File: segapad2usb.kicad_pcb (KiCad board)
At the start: 2 copper layers, 55 x 90 mm, 14 parts, among them J1 DB9_MALE_SEGA, J2 Conn_02x04_Odd_Even, SW1 RST, U1 Arduino_Pro_Micro

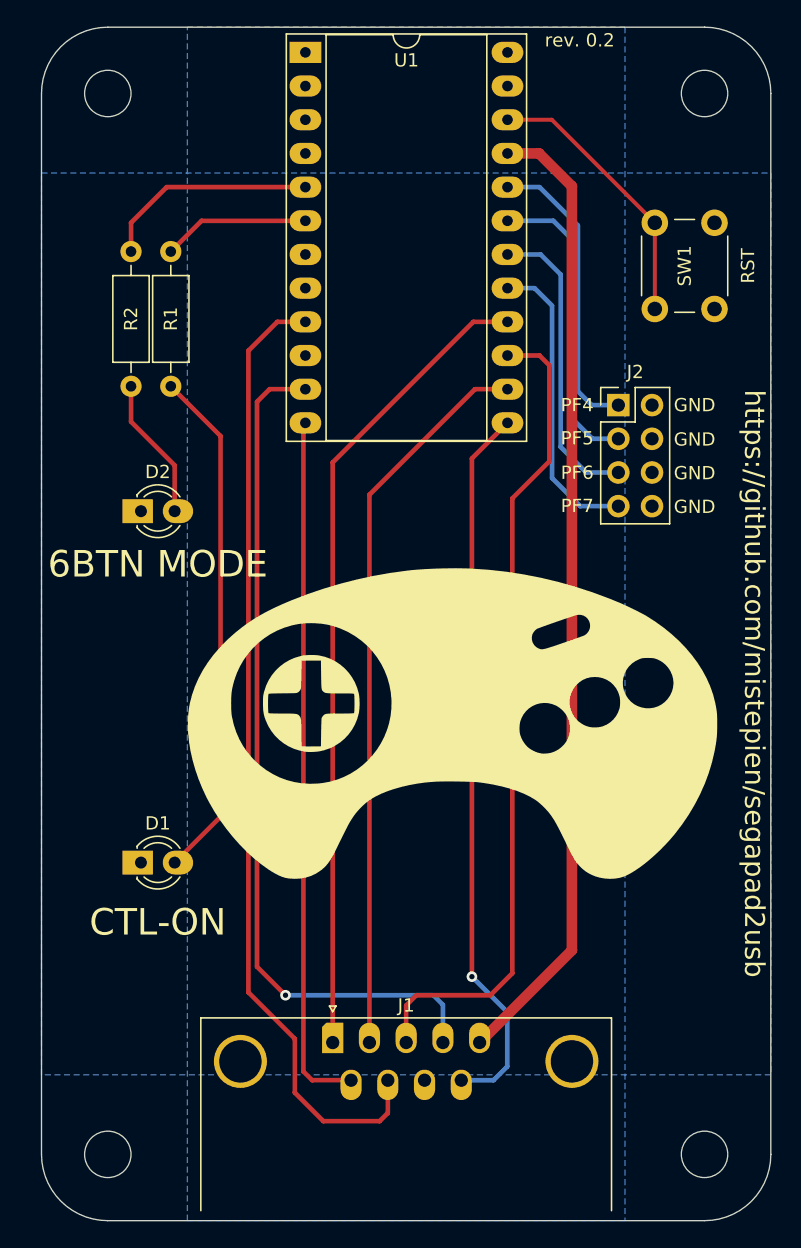
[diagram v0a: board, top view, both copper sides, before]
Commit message: PCB Rev. 0.4
- GND zone on both sides of pcb
- status led
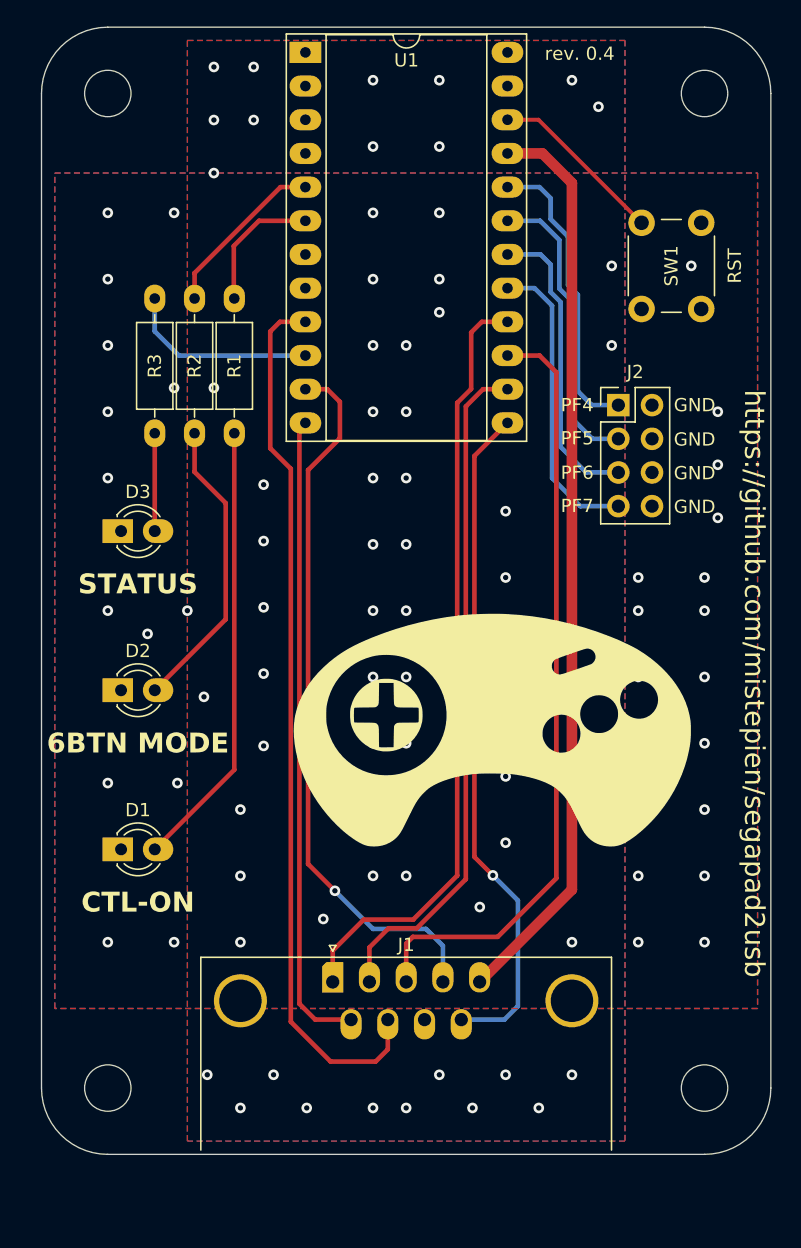
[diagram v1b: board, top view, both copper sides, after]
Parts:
- removed the G*** at (91.0, 98.5)
- added D3: STATUS, misc:LED_D3.0mm_Oval, F.Cu at (66.0, 84.0)
- added G***: LOGO, misc:md_gamepad_30x17mm, F.Cu at (94.0, 99.0)
- added R3: RxΩ, misc:R_Axial_DIN0207_L6.3mm_D2.5mm_P10.16mm_Horizontal_Oval, F.Cu at (68.5, 66.5)
- D1, D2: footprint Misc:LED_D3.0mm_Oval -> misc:LED_D3.0mm_Oval
- R1, R2: value R470Ω -> RxΩ; footprint Resistor_THT:R_Axial_DIN0207_L6.3mm_D2.5mm_P10.16mm_Horizontal -> misc:R_Axial_DIN0207_L6.3mm_D2.5mm_P10.16mm_Horizontal_Oval
- moved H1 91.8 mm to (110.0, 51.0)
- moved H3 87.5 mm to (110.0, 126.0)
- moved H4 45.3 mm to (65.0, 126.0)
- moved H2 45.0 mm to (65.0, 51.0)
- moved D2 13.6 mm to (66.0, 96.0)
- moved REF** 6.31 mm to (89.4, 95.1)
- moved R1 5.96 mm to (74.5, 66.5)
- moved R2 5.96 mm to (71.5, 66.5)
- moved J1 4.57 mm to (82.0, 118.0)
- moved D1 1.80 mm to (66.0, 108.0)
- moved SW1 1.00 mm to (105.2, 67.2)
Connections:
- U1 pad 10: unconnected-(U1-Pad10) -> /STATUSLED
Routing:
- net /STATUSLED: track 0.00 -> 14.6 mm
- net Net-(D2-A): track 10.8 -> 22.6 mm
- net /DB9_PIN_4: track 64.7 -> 54.3 mm
- net /RST: track 21.0 -> 13.3 mm
- net Net-(D3-A): track 0.00 -> 7.38 mm
- net /DB9_SELECT_PIN: track 73.2 -> 66.8 mm
- net Net-(D1-A): track 38.9 -> 34.0 mm
- net /DB9_PIN_6: track 52.8 -> 48.4 mm
- net VCC: track 73.3 -> 68.9 mm
- net /DB9_PIN_2: track 55.0 -> 51.3 mm
- net /DB9_PIN_3: track 62.3 -> 58.6 mm
- net /DB9_PIN_9: track 54.6 -> 51.1 mm
- net /MODELED: track 16.4 -> 13.0 mm
- net /DB9_PIN_1: track 61.3 -> 58.6 mm
- net /CTL-LED: track 11.1 -> 10.2 mm
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- added copper zone on F.Cu, net GND
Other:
- board size 55 x 90 mm -> 55 x 85 mm

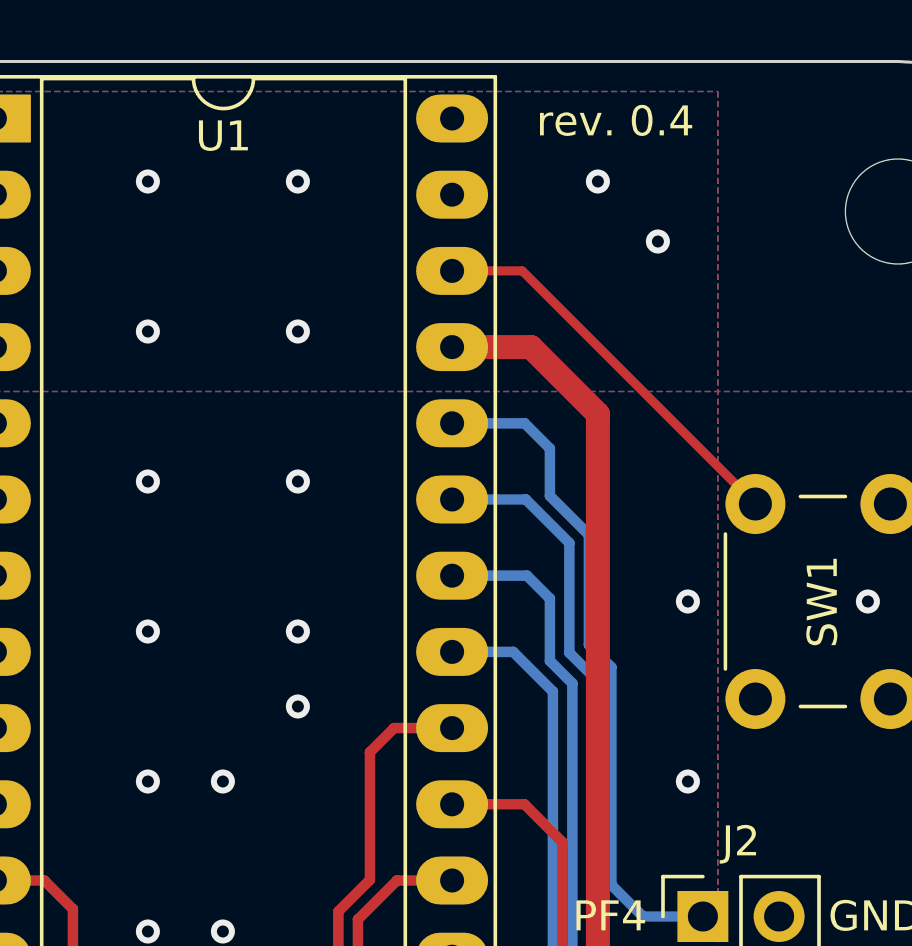
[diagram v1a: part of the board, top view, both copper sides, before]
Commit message: PCB Rev. 0.5
pcb will be cheaper in JLCPCB
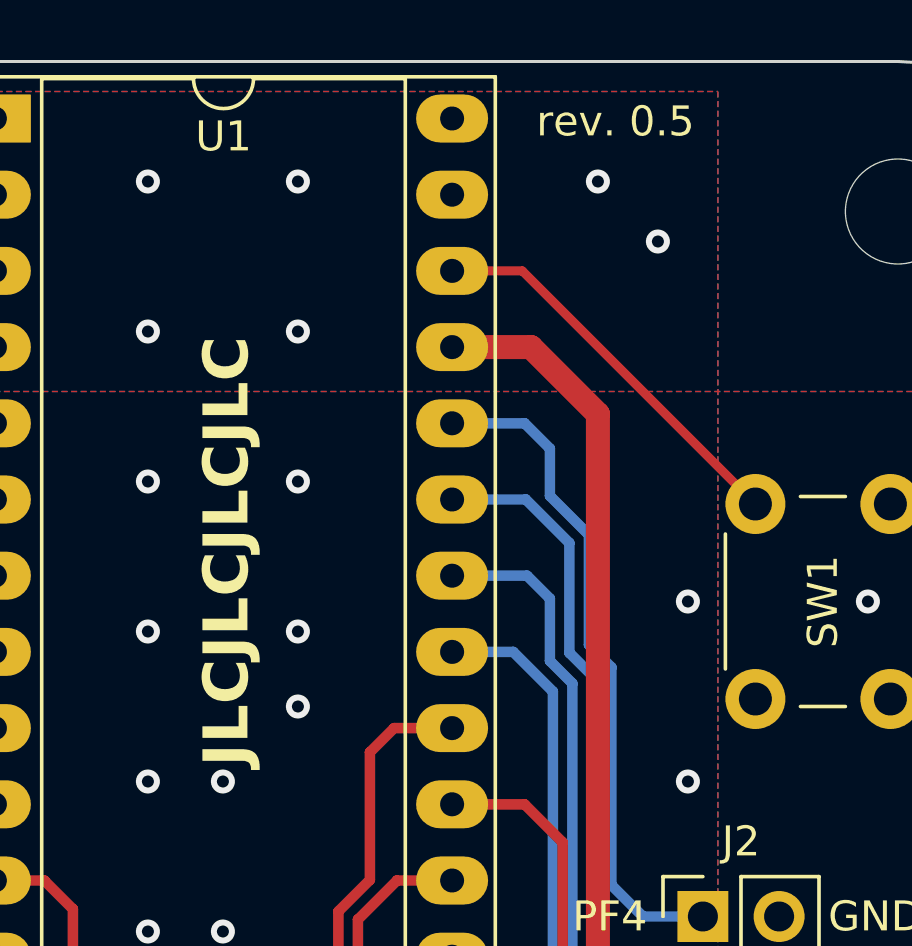
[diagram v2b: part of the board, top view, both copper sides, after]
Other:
- board text added: "JLCJLCJLCJLC"
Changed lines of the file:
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@@
   (title_block
     (title "segapad2usb")
-    (rev "0.4")
-    (company "mistepien")
+    (rev "0.5")
+    (company "mistepien@wp.pl")
   )
   (layers
@@
     (effects (font (size 1 1) (thickness 0.15)))
   )
+  (gr_text "JLCJLCJLCJLC" (at 88.5 69.5 90) (layer "F.SilkS")
+    (effects (font (size 1.5 1.5) (thickness 0.3) bold) (justify left bottom))
+  )
   (dimension (type aligned) (layer "Dwgs.User")

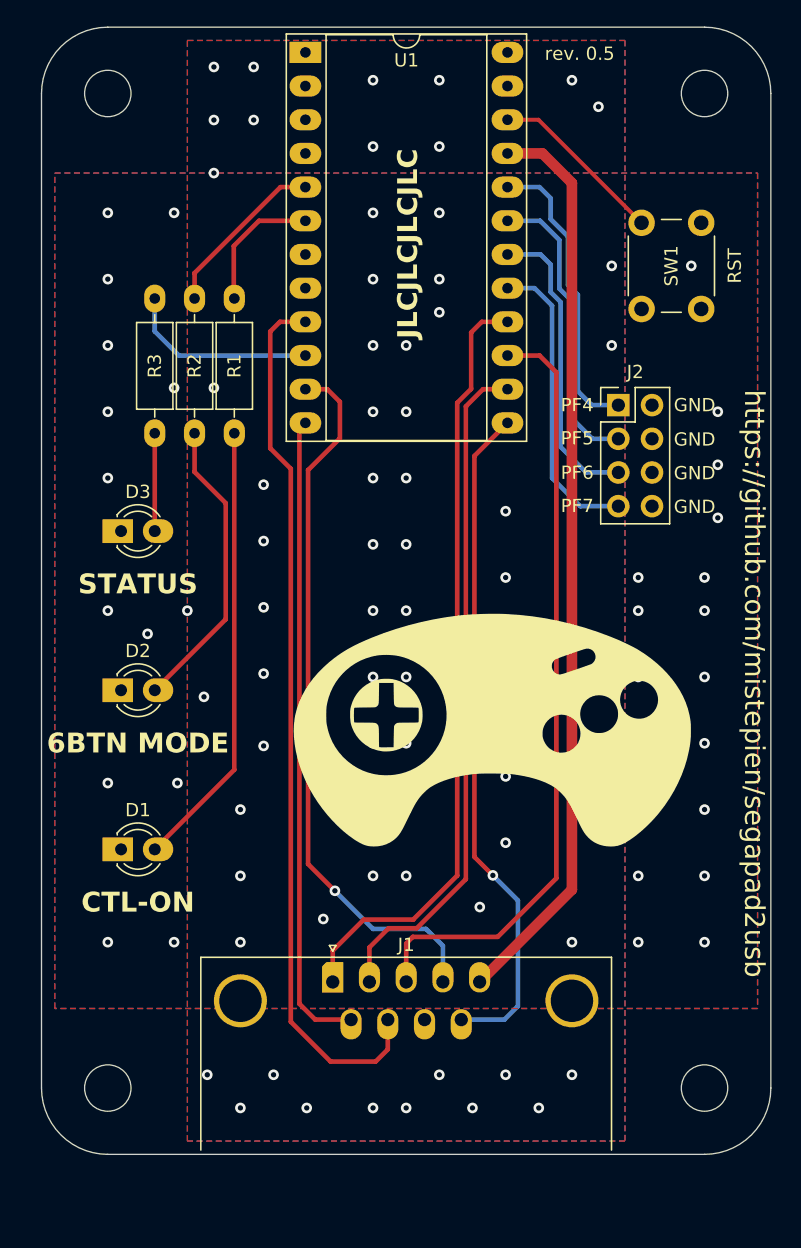
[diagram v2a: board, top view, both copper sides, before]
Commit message: added teardrops
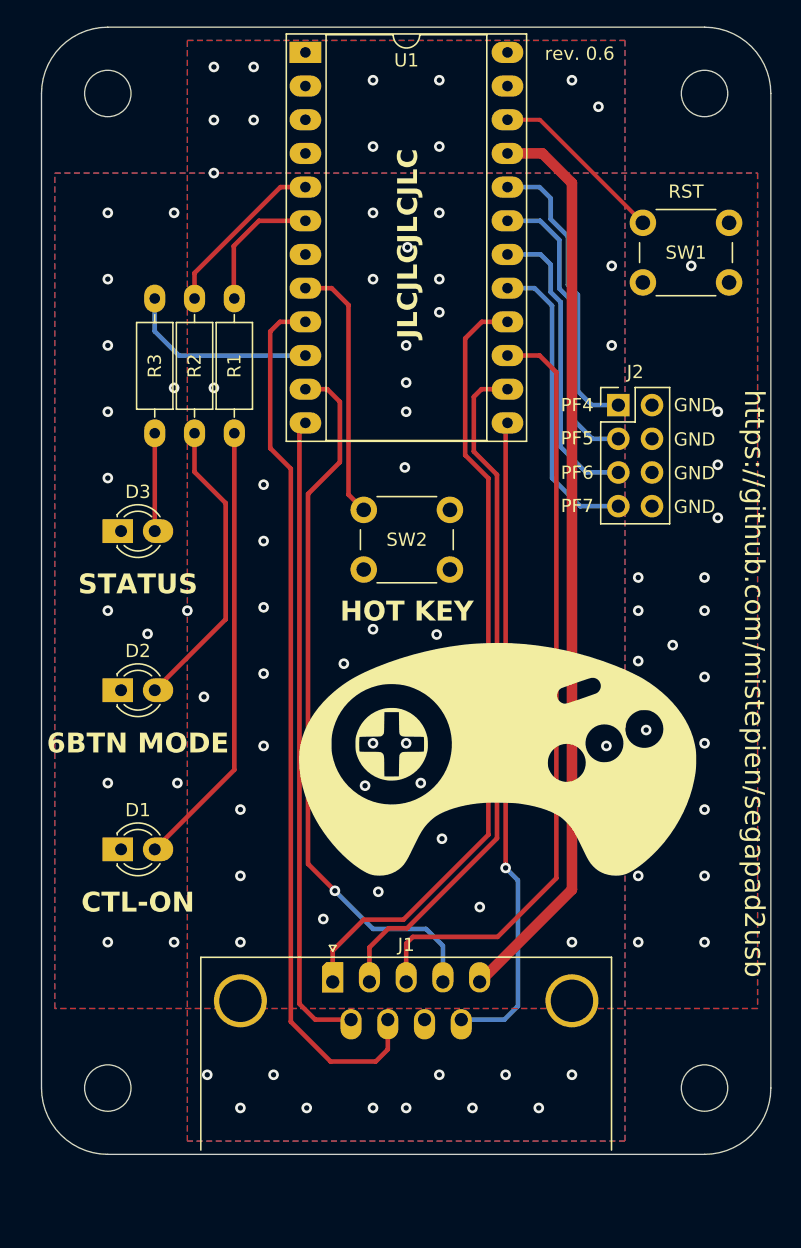
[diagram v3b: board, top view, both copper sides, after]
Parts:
- removed REF**: OSHW-Logo_28.5x30mm_SilkScreen, Symbol:OSHW-Logo_28.5x30mm_SilkScreen
- added SW2: HOT KEY, Button_Switch_THT:SW_PUSH_6mm_H4.3mm, F.Cu at (84.3, 82.4)
- moved SW1 6.50 mm to (105.3, 60.8), turned to 0 degrees
- moved G*** 2.24 mm to (94.4, 101.2)
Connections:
- U1 pad 8: unconnected-(U1-Digital5/PC6-Pad8) -> Net-(SW2-A)
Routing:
- net Net-(SW2-A): track 0.00 -> 19.7 mm
- net /DB9_PIN_9: track 51.1 -> 49.1 mm
- net /DB9_PIN_2: track 51.3 -> 52.4 mm
- net /DB9_PIN_1: track 58.6 -> 59.6 mm
- net GND: vias 98 -> 89
